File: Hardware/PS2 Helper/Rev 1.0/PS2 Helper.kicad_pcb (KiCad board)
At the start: 2 copper layers, 50 x 50 mm, 13 parts, among them J1 PORT, J2 KEYBOARD, U1 74HC595, U2 ATtiny85

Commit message: Housekeeping
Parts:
- G***: footprint 6502 Logos:6502 Keyboard Helper 5mm -> 6502 Logos:6502 PS2 Helper 5mm
- moved G*** 2.85 mm to (113.6, 93.3)

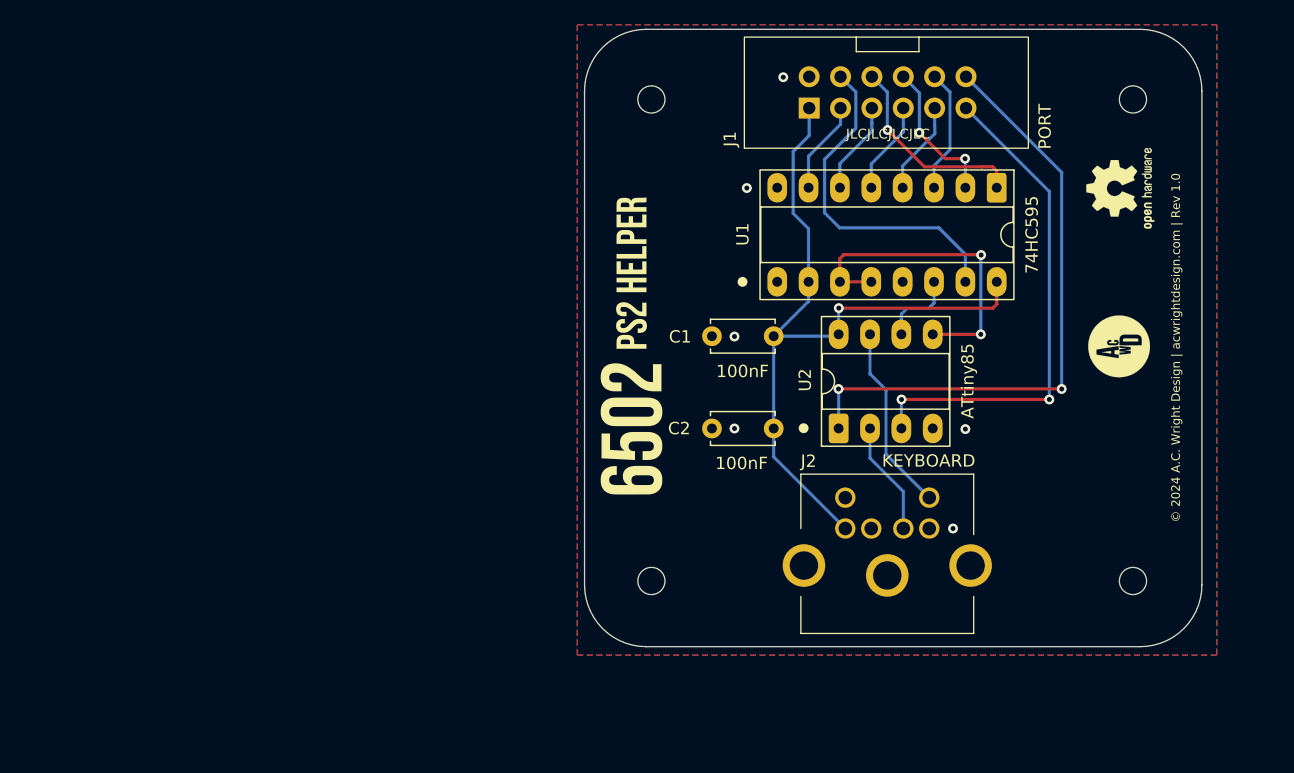
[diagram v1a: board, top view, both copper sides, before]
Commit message: Start work on PS2 Helper
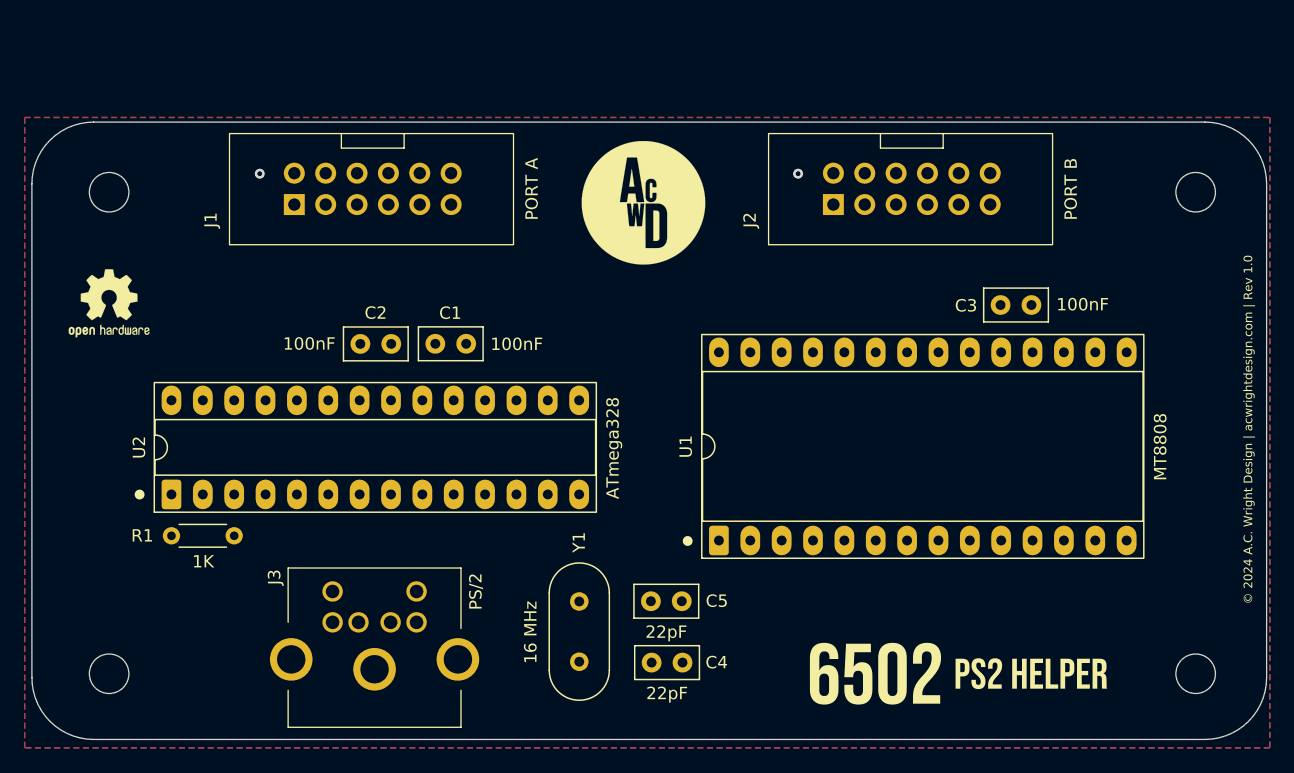
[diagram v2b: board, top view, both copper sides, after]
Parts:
- removed the G*** at (153.1, 101.3)
- removed the REF** at (154.2, 81.3)
- removed the REF** at (115.2, 81.3)
- removed the REF** at (154.2, 120.3)
- removed the REF** at (115.2, 120.3)
- added C3: 100nF, Capacitor_THT:C_Disc_D5.0mm_W2.5mm_P2.50mm, F.Cu at (143.5, 98.0)
- added C4: 22pF, Capacitor_THT:C_Disc_D5.0mm_W2.5mm_P2.50mm, F.Cu at (115.2, 126.9)
- added C5: 22pF, Capacitor_THT:C_Disc_D5.0mm_W2.5mm_P2.50mm, F.Cu at (115.2, 121.9)
- added G***: LOGO, A.C. Wright Logo:A.C. Wright Logo 10mm, F.Cu at (114.6, 89.7)
- added J3: PS/2, 6502 Parts:KMDGX-6S-BS, F.Cu at (94.1, 123.7)
- added R1: 1K, Resistor_THT:R_Axial_DIN0204_L3.6mm_D1.6mm_P5.08mm_Horizontal, F.Cu at (76.3, 116.6)
- added REF**: MountingHole_3.2mm_M3, MountingHole:MountingHole_3.2mm_M3, F.Cu at (159.3, 88.8)
- added REF**: MountingHole_3.2mm_M3, MountingHole:MountingHole_3.2mm_M3, F.Cu at (159.3, 127.8)
- added REF**: MountingHole_3.2mm_M3, MountingHole:MountingHole_3.2mm_M3, F.Cu at (71.3, 88.8)
- added REF**: MountingHole_3.2mm_M3, MountingHole:MountingHole_3.2mm_M3, F.Cu at (71.3, 127.8)
- added Y1: 16 MHz, Crystal:Crystal_HC49-U_Vertical, F.Cu at (109.4, 122.0)
- C1, C2: footprint Capacitor_THT:C_Disc_D5.0mm_W2.5mm_P5.00mm -> Capacitor_THT:C_Disc_D5.0mm_W2.5mm_P2.50mm
- J1: value PORT -> PORT A
- J2: value KEYBOARD -> PORT B; footprint 6502 Parts:KMDGX-6S-BS -> 6502 Parts:6502 GPIO Connector
- U1: value 74HC595 -> MT8808; footprint Package_DIP:DIP-16_W7.62mm_Socket_LongPads -> Package_DIP:DIP-28_W15.24mm_Socket_LongPads
- U2: value ATtiny85 -> ATmega328; footprint Package_DIP:DIP-8_W7.62mm_Socket_LongPads -> Package_DIP:DIP-28_W7.62mm_Socket_LongPads
- moved REF** 82.4 mm to (71.3, 97.8), turned to 0 degrees
- moved U2 54.3 mm to (76.3, 113.3)
- moved G*** 48.7 mm to (148.0, 127.8), turned to 0 degrees
- moved J1 42.4 mm to (86.3, 89.8)
- moved U1 36.4 mm to (120.7, 117.0), turned to 90 degrees
- moved C2 34.2 mm to (91.7, 101.1), turned to 0 degrees
- moved J2 26.8 mm to (130.0, 89.8), turned to 90 degrees
- moved C1 24.9 mm to (100.2, 101.1)
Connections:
- C1 pad 1: VCC -> GND
- C1 pad 2: GND -> VCC
- C2 pad 1: VCC -> GND
- C2 pad 2: GND -> Net-(U2-AREF)
- J1 pad 11: CA1 -> unconnected-(J1-Pin_11-Pad11)
- J1 pad 12: CA2 -> unconnected-(J1-Pin_12-Pad12)
- J2 pad 1: KBD_DATA -> VCC
- J2 pad 2: unconnected-(J2-Pad2) -> GND
- J2 pad 3: GND -> PB7
- J2 pad 5: VCC -> PB6
- J2 pad 6: KBD_CLK -> PB1
- J2 pad 8: unconnected-(J2-Pad8) -> PB2
- U1 pad 1: PA1 -> AY2
- U1 pad 10: VCC -> RESET
- U1 pad 11: CLK -> PB7
- U1 pad 12: CLK -> PB6
- U1 pad 13: GND -> PB5
- U1 pad 14: DATA -> PB4
- U1 pad 15: PA0 -> PB3
- U1 pad 16: VCC -> PB2
- U1 pad 2: PA2 -> STROBE
- U1 pad 3: PA3 -> GND
- U1 pad 4: PA4 -> DATA
- U1 pad 5: PA5 -> GND
- U1 pad 6: PA6 -> PA0
- U1 pad 7: PA7 -> PA2
- U1 pad 8: GND -> PA4
- U1 pad 9: unconnected-(U1-QH&apos;-Pad9) -> PA6
- U2 pad 1: CA2 -> Net-(U2-~{RESET}/PC6)
- U2 pad 2: KBD_DATA -> unconnected-(U2-PD0-Pad2)
- U2 pad 3: CA1 -> unconnected-(U2-PD1-Pad3)
- U2 pad 4: GND -> PS2CLK
- U2 pad 5: CLK -> PS2DATA
- U2 pad 6: DATA -> unconnected-(U2-PD4-Pad6)
- U2 pad 7: KBD_CLK -> VCC
- U2 pad 8: VCC -> GND
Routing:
- net VCC: track 60.9 -> 0.00 mm, vias 1 -> 0
- net CA2: track 49.8 -> 0.00 mm, vias 2 -> 0
- net CA1: track 40.7 -> 0.00 mm, vias 2 -> 0
- net PA0: track 27.6 -> 0.00 mm
- net CLK: track 26.3 -> 0.00 mm, vias 2 -> 0
- net PA1: track 16.4 -> 0.00 mm, vias 1 -> 0
- net KBD_CLK: track 15.2 -> 0.00 mm
- net PA2: track 12.0 -> 0.00 mm, vias 2 -> 0
- net PA3: track 10.0 -> 0.00 mm
- net KBD_DATA: track 9.22 -> 0.00 mm
- net PA4: track 7.54 -> 0.00 mm
- net PA5: track 7.53 -> 0.00 mm
- net PA6: track 7.52 -> 0.00 mm
- net PA7: track 7.52 -> 0.00 mm
- net DATA: track 6.38 -> 0.00 mm
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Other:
- board size 50 x 50 mm -> 100 x 50 mm
- board text removed: "JLCJLCJLCJLC"

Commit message: Add PS2 Helper PCB
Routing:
- net VCC: track 0.00 -> 117.6 mm, vias 0 -> 4
- net PA6: track 0.00 -> 75.5 mm, vias 0 -> 2
- net PA0: track 0.00 -> 72.9 mm, vias 0 -> 2
- net PA2: track 0.00 -> 70.3 mm, vias 0 -> 2
- net PA4: track 0.00 -> 68.3 mm, vias 0 -> 2
- net PA7: track 0.00 -> 62.9 mm, vias 0 -> 2
- net PA5: track 0.00 -> 60.1 mm, vias 0 -> 4
- net PA1: track 0.00 -> 55.8 mm, vias 0 -> 4
- net AY2: track 0.00 -> 55.7 mm, vias 0 -> 2
- net AY1: track 0.00 -> 55.1 mm, vias 0 -> 2
- net AY0: track 0.00 -> 53.6 mm, vias 0 -> 2
- net AX2: track 0.00 -> 52.1 mm, vias 0 -> 2
- net RESET: track 0.00 -> 52.0 mm, vias 0 -> 2
- net PB6: track 0.00 -> 52.0 mm, vias 0 -> 4
- net PB7: track 0.00 -> 51.8 mm, vias 0 -> 4
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
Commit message: Housekeeping
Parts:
- H1, H2, H3, H4: renamed from REF**; value MountingHole_3.2mm_M3 -> MountingHole
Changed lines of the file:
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@@
 			)
 		)
-		(attr exclude_from_pos_files exclude_from_bom)
+		(attr board_only exclude_from_pos_files exclude_from_bom allow_missing_courtyard)
 		(fp_poly
 			(pts
@@
 			)
 		)
-		(attr through_hole)
+		(attr through_hole board_only exclude_from_pos_files exclude_from_bom allow_missing_courtyard)
 		(fp_poly
 			(pts
@@
 		(descr "Mounting Hole 3.2mm, no annular, M3")
 		(tags "mounting hole 3.2mm no annular m3")
-		(property "Reference" "REF**"
+		(property "Reference" "H2"
 			(at 0 -4.2 0)
 			(layer "F.SilkS")
@@
 			)
 		)
-		(property "Value" "MountingHole_3.2mm_M3"
+		(property "Value" "MountingHole"
 			(at 0 4.2 0)
 			(layer "F.Fab")
@@
 			)
 		)
-		(property "Datasheet" ""
+		(property "Datasheet" "~"
 			(at 0 0 0)
 			(unlocked yes)
@@
 			)
 		)
-		(property "Description" ""
+		(property "Description" "Mounting Hole without connection"
 			(at 0 0 0)
 			(unlocked yes)
@@
 			)
 		)
-		(attr exclude_from_pos_files exclude_from_bom)
+		(property ki_fp_filters "MountingHole*")
+		(sheetname "/")
+		(sheetfile "PS2 Helper.kicad_sch")
+		(attr board_only exclude_from_pos_files exclude_from_bom)
 		(fp_circle
 			(center 0 0)
@@
 			)
 		)
-		(property "Datasheet" ""
+		(property "Datasheet" "http://ww1.microchip.com/downloads/en/DeviceDoc/ATmega328_P%20AVR%20MCU%20with%20picoPower%20Technology%20Data%20Sheet%2040001984A.pdf"
 			(at 0 0 90)
 			(layer "F.Fab")
@@
 			)
 		)
-		(property "Description" ""
+		(property "Description" "20MHz, 32kB Flash, 2kB SRAM, 1kB EEPROM, DIP-28"
 			(at 0 0 90)
 			(layer "F.Fab")
@@
 			)
 		)
-		(attr board_only exclude_from_pos_files exclude_from_bom)
+		(attr board_only exclude_from_pos_files exclude_from_bom allow_missing_courtyard)
 		(fp_poly
 			(pts
@@
 		(descr "Mounting Hole 3.2mm, no annular, M3")
 		(tags "mounting hole 3.2mm no annular m3")
-		(property "Reference" "REF**"
+		(property "Reference" "H4"
 			(at 0 -4.2 0)
 			(layer "F.SilkS")
@@
 			)
 		)
-		(property "Value" "MountingHole_3.2mm_M3"
+		(property "Value" "MountingHole"
 			(at 0 4.2 0)
 			(layer "F.Fab")
@@
 			)
 		)
-		(property "Datasheet" ""
+		(property "Datasheet" "~"
 			(at 0 0 0)
 			(unlocked yes)
@@
 			)
 		)
-		(property "Description" ""
+		(property "Description" "Mounting Hole without connection"
 			(at 0 0 0)
 			(unlocked yes)
@@
 			)
 		)
-		(attr exclude_from_pos_files exclude_from_bom)
+		(property ki_fp_filters "MountingHole*")
+		(sheetname "/")
+		(sheetfile "PS2 Helper.kicad_sch")
+		(attr board_only exclude_from_pos_files exclude_from_bom)
 		(fp_circle
 			(center 0 0)
@@
 		(descr "Mounting Hole 3.2mm, no annular, M3")
 		(tags "mounting hole 3.2mm no annular m3")
-		(property "Reference" "REF**"
+		(property "Reference" "H1"
 			(at 0 -4.2 0)
 			(layer "F.SilkS")
@@
 			)
 		)
-		(property "Value" "MountingHole_3.2mm_M3"
+		(property "Value" "MountingHole"
 			(at 0 4.2 0)
 			(layer "F.Fab")
@@
 			)
 		)
-		(property "Datasheet" ""
+		(property "Datasheet" "~"
 			(at 0 0 0)
 			(unlocked yes)
@@
 			)
 		)
-		(property "Description" ""
+		(property "Description" "Mounting Hole without connection"
 			(at 0 0 0)
 			(unlocked yes)
@@
 			)
 		)
-		(attr exclude_from_pos_files exclude_from_bom)
+		(property ki_fp_filters "MountingHole*")
+		(sheetname "/")
+		(sheetfile "PS2 Helper.kicad_sch")
+		(attr board_only exclude_from_pos_files exclude_from_bom)
 		(fp_circle
 			(center 0 0)
@@
 		(descr "Mounting Hole 3.2mm, no annular, M3")
 		(tags "mounting hole 3.2mm no annular m3")
-		(property "Reference" "REF**"
+		(property "Reference" "H3"
 			(at 0 -4.2 0)
 			(layer "F.SilkS")
@@
 			)
 		)
-		(property "Value" "MountingHole_3.2mm_M3"
+		(property "Value" "MountingHole"
 			(at 0 4.2 0)
 			(layer "F.Fab")
@@
 			)
 		)
-		(property "Datasheet" ""
+		(property "Datasheet" "~"
 			(at 0 0 0)
 			(unlocked yes)
@@
 			)
 		)
-		(property "Description" ""
+		(property "Description" "Mounting Hole without connection"
 			(at 0 0 0)
 			(unlocked yes)
@@
 			)
 		)
-		(attr exclude_from_pos_files exclude_from_bom)
+		(property ki_fp_filters "MountingHole*")
+		(sheetname "/")
+		(sheetfile "PS2 Helper.kicad_sch")
+		(attr board_only exclude_from_pos_files exclude_from_bom)
 		(fp_circle
 			(center 0 0)
@@
 			)
 		)
-		(property "Mouser" "774-MP107-E"
+		(property "Digikey" "3155-16M20P2/49US-ND"
 			(at 0 0 270)
 			(unlocked yes)

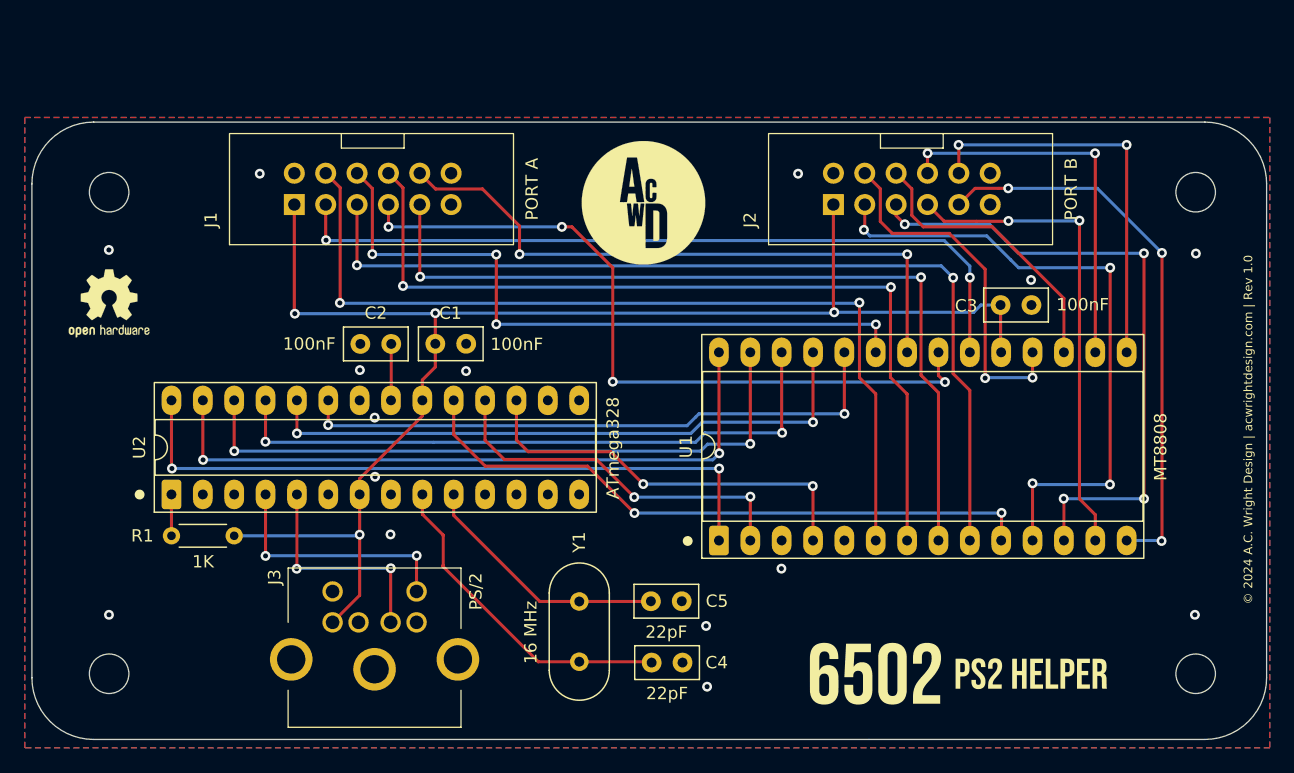
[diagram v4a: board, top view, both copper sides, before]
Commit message: Add joystick port to PS2 Helper
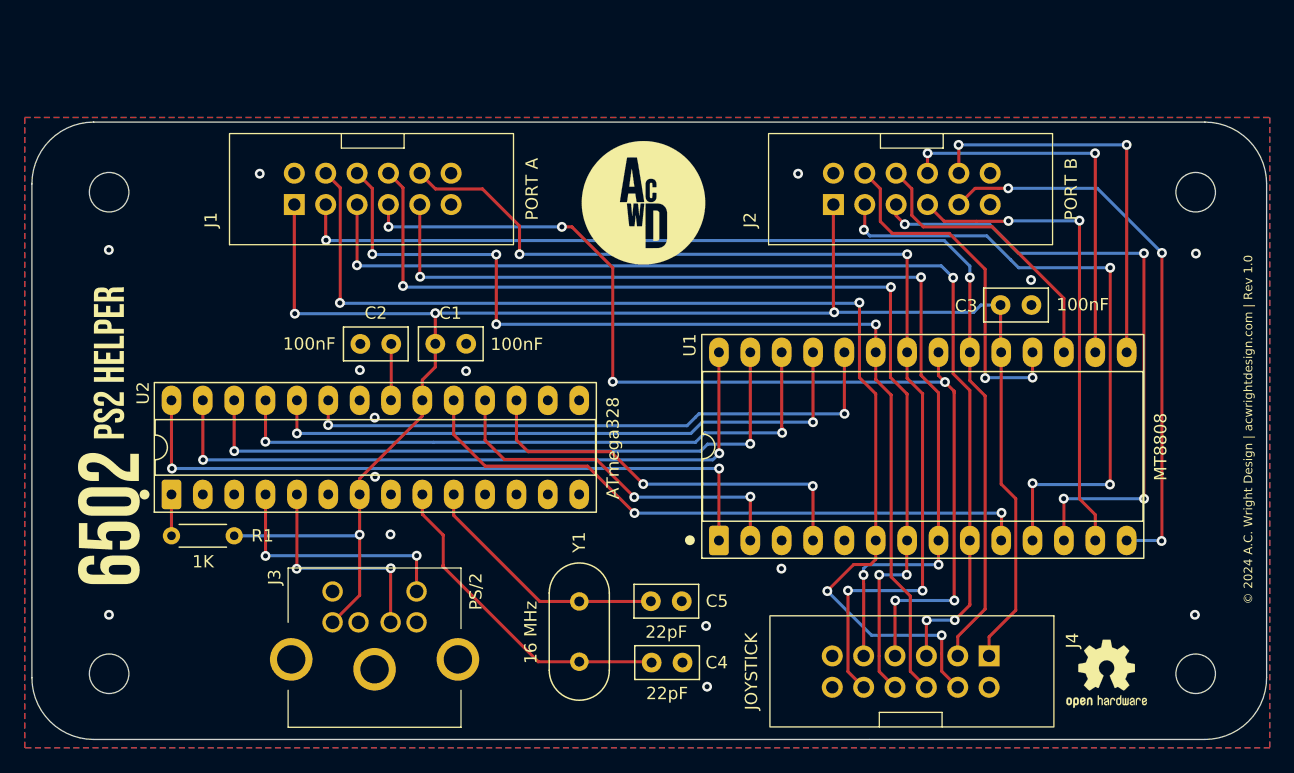
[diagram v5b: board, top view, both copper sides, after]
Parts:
- added J4: JOYSTICK, 6502 Parts:6502 GPIO Connector, F.Cu at (142.6, 126.4)
- moved REF** 86.2 mm to (152.1, 127.8)
- moved G*** 81.5 mm to (71.3, 100.6), turned to 90 degrees
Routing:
- net PA3: track 51.5 -> 85.7 mm, vias 2 -> 4
- net PA1: track 55.8 -> 84.6 mm
- net PA5: track 60.1 -> 87.4 mm, vias 4 -> 6
- net PA7: track 62.9 -> 88.9 mm
- net VCC: track 117.6 -> 143.6 mm
- net PA0: track 72.9 -> 95.0 mm, vias 2 -> 4
- net PA4: track 68.3 -> 83.6 mm, vias 2 -> 4
- net PA2: track 70.3 -> 84.9 mm, vias 2 -> 4
- net PA6: track 75.5 -> 87.6 mm, vias 2 -> 4

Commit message: Add pullups to PS2 Helper
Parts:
- added R2: 1K, Resistor_THT:R_Axial_DIN0204_L3.6mm_D1.6mm_P5.08mm_Horizontal, F.Cu at (75.0, 94.6)
- added R3: 1K, Resistor_THT:R_Axial_DIN0204_L3.6mm_D1.6mm_P5.08mm_Horizontal, F.Cu at (82.0, 94.6)
- added R4: 1K, Resistor_THT:R_Axial_DIN0204_L3.6mm_D1.6mm_P5.08mm_Horizontal, F.Cu at (75.0, 96.7)
- added R5: 1K, Resistor_THT:R_Axial_DIN0204_L3.6mm_D1.6mm_P5.08mm_Horizontal, F.Cu at (82.0, 96.7)
- added R6: 1K, Resistor_THT:R_Axial_DIN0204_L3.6mm_D1.6mm_P5.08mm_Horizontal, F.Cu at (75.0, 98.8)
- added R7: 1K, Resistor_THT:R_Axial_DIN0204_L3.6mm_D1.6mm_P5.08mm_Horizontal, F.Cu at (82.0, 98.8)
- added R8: 1K, Resistor_THT:R_Axial_DIN0204_L3.6mm_D1.6mm_P5.08mm_Horizontal, F.Cu at (75.0, 100.9)
- added R9: 1K, Resistor_THT:R_Axial_DIN0204_L3.6mm_D1.6mm_P5.08mm_Horizontal, F.Cu at (82.0, 100.9)
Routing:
- net PA2: track 84.9 -> 118.2 mm, vias 4 -> 7
- net PA3: track 85.7 -> 113.6 mm, vias 4 -> 6
- net PA4: track 83.6 -> 109.2 mm, vias 4 -> 6
- net PA6: track 87.6 -> 109.7 mm, vias 4 -> 6
- net PA5: track 87.4 -> 106.6 mm, vias 6 -> 8
- net VCC: track 143.6 -> 162.6 mm, vias 4 -> 5
- net PA0: track 95.0 -> 113.3 mm, vias 4 -> 6
- net PA7: track 88.9 -> 104.1 mm, vias 2 -> 4
- net PA1: track 84.6 -> 95.9 mm
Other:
- board text added: "R2-R9"

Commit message: Production fixes
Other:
- board text added: "JLCJLCJLCJLC"
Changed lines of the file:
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@@
 		(layer "Edge.Cuts")
+	)
+	(gr_text "JLCJLCJLCJLC"
+		(at 137.2 109.4 0)
+		(layer "F.SilkS")
+		(effects
+			(font
+				(size 1 1)
+				(thickness 0.15)
+			)
+		)
 	)
 	(gr_text "© 2024 A.C. Wright Design | acwrightdesign.com | Rev 1.0"
